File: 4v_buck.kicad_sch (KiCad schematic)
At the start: 4 parts, among them U3 MIC28517T-E/PHA

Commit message: 4v buck updates
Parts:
- added C9: 4u7F 10V, BR_Passives:C_0402_1005Metric-minimized, symbol BR_Capacitors_0402:C_0402_4u7F_10V_X7T_20%
- added L1: 10uH 10A, BR_Inductors:XR1265-100M, symbol BR_Inductors:L_XR1265-100M
- added R21: 2k2, BR_Passives:R_0402_1005Metric-minimized, symbol BR_Resistors_0402:R_0402_2k2
- added R26: 10k, BR_Passives:C_0402_1005Metric-minimized, symbol BR_Resistors_0402:R_0402_10k
- added R38: 1k74, BR_Passives:C_0402_1005Metric-minimized, symbol BR_Resistors_0402:R_0402_1k74
- added R4, R5: 2R2, BR_Passives:R_0402_1005Metric-minimized, symbol BR_Resistors_0402:R_0402_2R2
- added R6: 100k, BR_Passives:C_0402_1005Metric-minimized, symbol BR_Resistors_0402:R_0402_100k
- added R8: 51k, BR_Passives:C_0402_1005Metric-minimized, symbol BR_Resistors_0402:R_0402_51k
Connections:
- net GND: now also R38.2, R8.2
- net PGND: now also C9.2
- net PVIN: now also R4.2, R6.1
- net at C2.2, U3.12 (SW), U3.13 (SW)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: now also L1.1, R21.1
- net at U3.1 (ILIM): now also R21.2
- net at U3.21 (PVDD): now also C9.1, R5.1
- net at U3.25 (FREQ): now also R6.2, R8.1
- net at U3.27 (FB): now also R26.2, R38.1
- net at C1.1, U3.30 (VDD): now also R5.2
- net at U3.31 (SVIN): now also R4.1
- new net VOUT: L1.2, R26.1
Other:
- moved on the sheet: C1

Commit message: 4v buck updates
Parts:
- added C19: 1uF 100V, BR_Passives:C_0805_2012Metric-minimized, symbol BR_Capacitors_0805:C_0805_1uF_100V_X7S_10%
- added C20: 10nF 50V, BR_Passives:C_0402_1005Metric-minimized, symbol BR_Capacitors_0402:C_0402_10nF_50V_X7R_10%
- added C21: 100nF 100V, BR_Passives:C_0402_1005Metric-minimized, symbol BR_Capacitors_0402:C_0402_100nF_100V_X5R_20%
- added R46: 15k, BR_Passives:C_0402_1005Metric-minimized, symbol BR_Resistors_0402:R_0402_15k
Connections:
- net GND: now also C1.2, U3.26 (MODE), C19.2
- net PGND: no longer C1.2, U3.26 (MODE)
- net VOUT: now also C20.1
- net at C2.2, L1.1, R21.1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: now also R46.2
- net at R26.2, R38.1, U3.27 (FB): now also C20.2, C21.2
- net at R4.1, U3.31 (SVIN): now also C19.1
- new net: C21.1, R46.1
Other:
- moved on the sheet: C9, R4

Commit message: 4v buck complete
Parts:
- added C22, C23, C24: 2u2F 100V, BR_Passives:C_0805_2012Metric-minimized, symbol BR_Capacitors_0805:C_0805_2u2F_100V_X7T_10%
- added C25, C26: 10uF 10V, BR_Passives:C_0603_1608Metric-minimized, symbol BR_Capacitors_0603:C_0603_10uF_10V_X7T_10%
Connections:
- net PGND: now also C22.2, C23.2, C24.2, C25.2, C26.2
- net PVIN: now also C22.1, C23.1, C24.1
- net VOUT: now also C25.1, C26.1
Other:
- moved on the sheet: L1

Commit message: power scheme updates
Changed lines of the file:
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@@
+	(wire
+		(pts
+			(xy 255.27 78.74) (xy 264.16 78.74)
+		)
+		(stroke
+			(width 0)
+			(type default)
+		)
+	)
 	(wire
 		(pts
@@
 	(wire
 		(pts
+			(xy 255.27 78.74) (xy 240.03 78.74)
+		)
+		(stroke
+			(width 0)
+			(type default)
+		)
+	)
+	(wire
+		(pts
 			(xy 224.79 78.74) (xy 240.03 78.74)
 		)
@@
 	(wire
 		(pts
-			(xy 240.03 78.74) (xy 255.27 78.74)
-		)
-		(stroke
-			(width 0)
-			(type default)
-		)
-	)
-	(wire
-		(pts
 			(xy 86.36 86.36) (xy 86.36 81.28)
 		)
@@
 		(pts
 			(xy 172.72 104.14) (xy 181.61 104.14)
-		)
-		(stroke
-			(width 0)
-			(type default)
-		)
-	)
-	(wire
-		(pts
-			(xy 255.27 78.74) (xy 264.16 78.74)
 		)
 		(stroke
@@
 	)
 	(label "4V"
-		(at 227.33 78.74 0)
+		(at 259.08 78.74 0)
 		(effects
 			(font

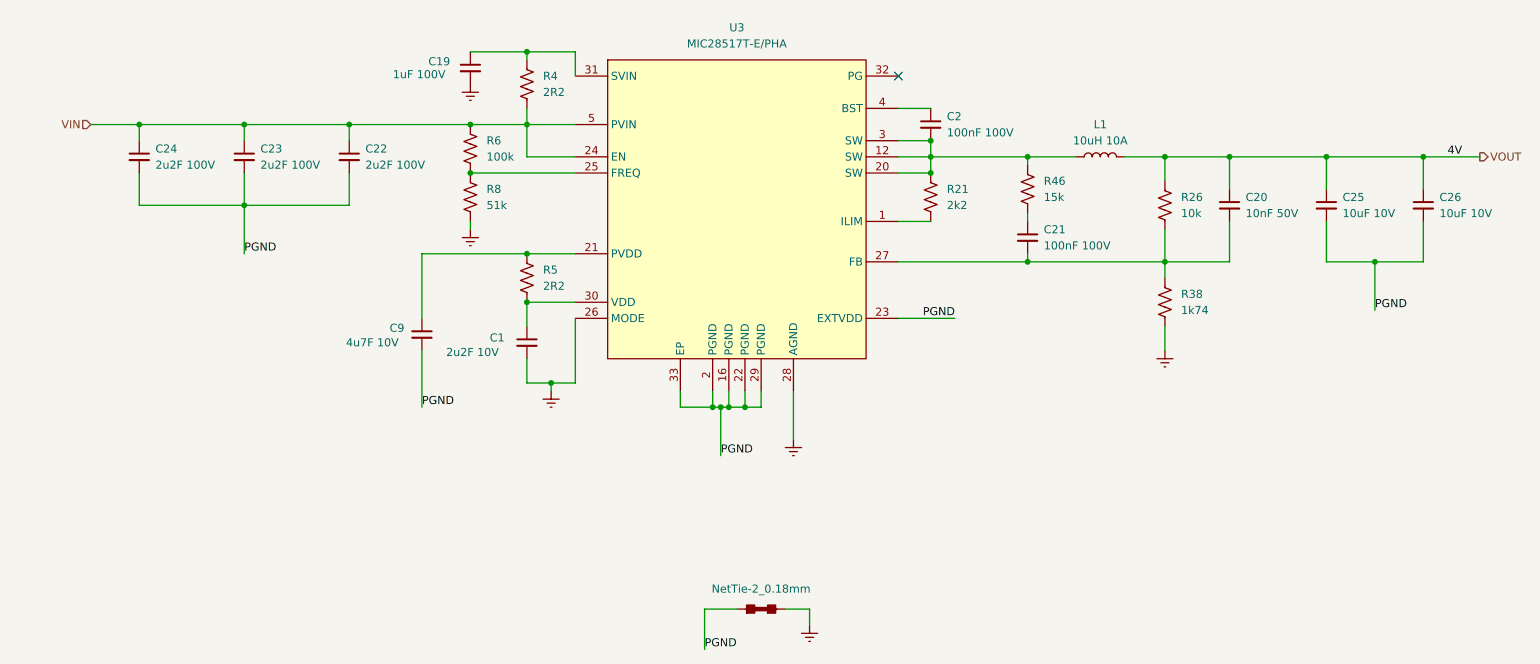
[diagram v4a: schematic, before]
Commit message: added annotations
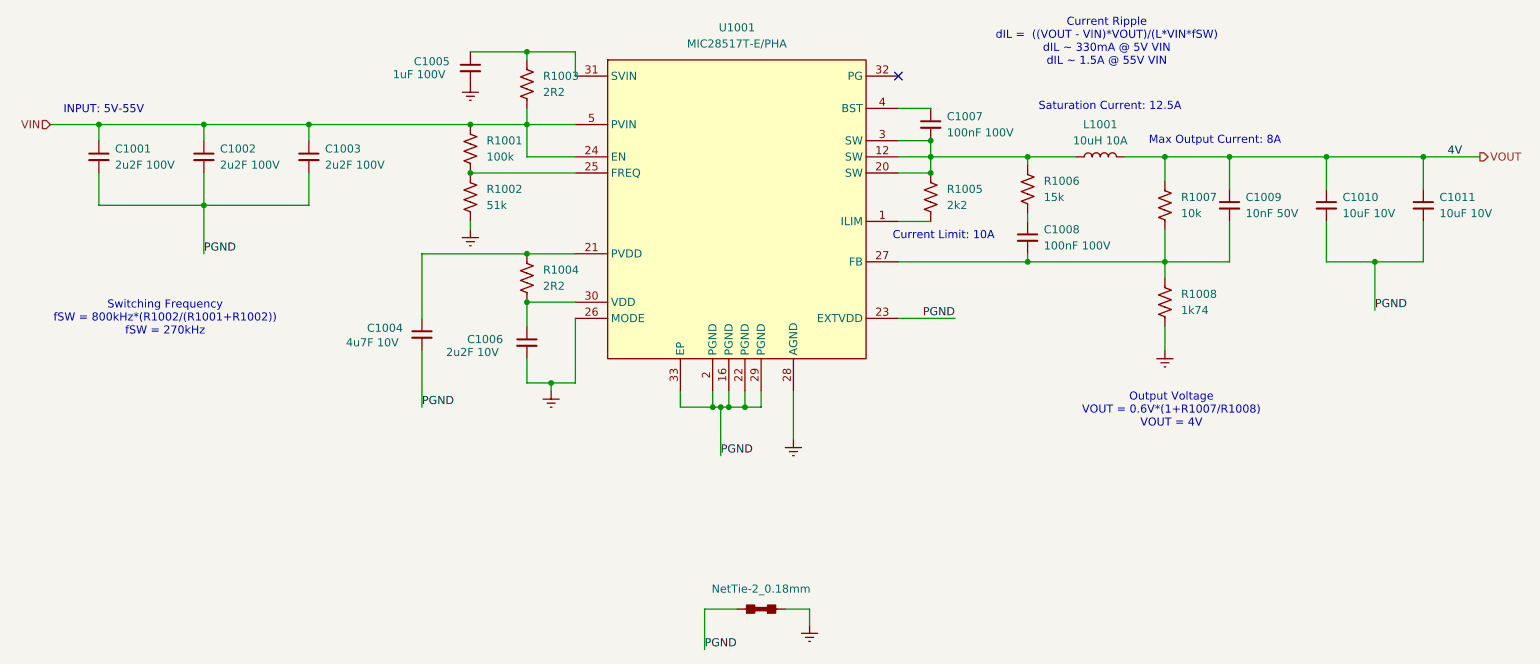
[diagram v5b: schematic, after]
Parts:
- renumbered C24 to C1001, C23 to C1002, C22 to C1003, C9 to C1004, C19 to C1005, C1 to C1006, C2 to C1007, C21 to C1008, C20 to C1009, C25 to C1010, C26 to C1011, L1 to L1001, NT1 to NT1001, R6 to R1001, R8 to R1002, R4 to R1003, R5 to R1004, R21 to R1005, R46 to R1006, R26 to R1007, R38 to R1008, U3 to U1001
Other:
- note added: "Current Limit: 10A"
- note added: "Current Ripple dIL = ((VOUT - VIN)*VOUT)/(L*VIN*fSW) dIL ~ 330mA @ 5V VIN dIL ~ 1.5A @ 55V VIN"
- note added: "INPUT: 5V-55V"
- note added: "Max Output Current: 8A"
- note added: "Output Voltage VOUT = 0.6V*(1+R1007/R1008) VOUT = 4V"
- note added: "Saturation Current: 12.5A"
- note added: "Switching Frequency fSW = 800kHz*(R1002/(R1001+R1002)) fSW = 270kHz"
- moved on the sheet: C1001, C1002, C1003

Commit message: ripple injection updates
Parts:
- C1009: value 10nF 50V -> 4n7F 100V; footprint BR_Passives:C_0402_1005Metric-minimized -> BR_Passives:C_0402_1005Metric; symbol BR_Capacitors_0402:C_0402_10nF_50V_X7R_10% -> BR_Capacitors_0402:C_0402_4n7F_100V_X7R_10%; BRE Number BRE-000013 -> BRE-000032; JLCPCB Part Num C60133 -> C415704; Manufacturer YAGEO -> Murata Electronics; Manufacturer Part Num CC0402KRX7R9BB103 -> GRM155R72A472KA01D; Supplier Part Num 1 311-1349-1-ND -> 490-3885-1-ND; Supplier Part Num 2 603-CC402KRX7R9BB103 -> 81-GRM155R72A472KA01; Supplier Part Num 3 C60133 -> C415704
- R1006: value 15k -> 24k9; symbol BR_Resistors_0402:R_0402_15k -> BR_Resistors_0402:R_0402_24k9; BRE Number BRE-000304 -> BRE-001239; JLCPCB Part Num C144795 -> C138027; Manufacturer Part Num AC0402FR-0715KL -> RC0402FR-0724K9L; Supplier Part Num 1 YAG3444CT-ND -> 311-24.9KLRCT-ND; Supplier Part Num 2 YAG3444TR-ND -> 311-24.9KLRCT-ND; Supplier Part Num 3 C144795 -> C138027
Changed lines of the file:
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@@
 	)
 	(symbol
-		(lib_id "BR_Capacitors_0402:C_0402_10nF_50V_X7R_10%")
+		(lib_id "BR_Capacitors_0402:C_0402_4n7F_100V_X7R_10%")
 		(at 224.79 86.36 0)
 		(unit 1)
@@
 			)
 		)
-		(property "Value" "10nF 50V"
+		(property "Value" "4n7F 100V"
 			(at 227.33 87.6362 0)
 			(effects
@@
 			)
 		)
-		(property "Footprint" "BR_Passives:C_0402_1005Metric-minimized"
+		(property "Footprint" "BR_Passives:C_0402_1005Metric"
 			(at 224.79 10.16 0)
 			(effects
@@
 			)
 		)
-		(property "Datasheet" "https://www.yageo.com/upload/media/product/productsearch/datasheet/mlcc/UPY-GPHC_X7R_6.3V-to-250V_23.pdf"
+		(property "Datasheet" "https://www.lcsc.com/datasheet/lcsc_datasheet_2304140030_Murata-Electronics-GRM155R72A472KA01D_C415704.pdf"
 			(at 224.79 12.7 0)
 			(effects
@@
 			)
 		)
-		(property "Description" "10nF 50V X7R 10% Ceramic Capacitor 0402"
+		(property "Description" "4.7nF 100V X7R 10% Ceramic Capacitor 0402"
+			(at 224.79 22.86 0)
+			(effects
+				(font
+					(size 1.27 1.27)
+				)
+				(justify left)
+				(hide yes)
+			)
+		)
+		(property "Manufacturer" "Murata Electronics"
 			(at 224.79 15.24 0)
 			(effects
@@
 			)
 		)
-		(property "Manufacturer" "YAGEO"
+		(property "Manufacturer Part Num" "GRM155R72A472KA01D"
 			(at 224.79 17.78 0)
 			(effects
@@
 			)
 		)
-		(property "Manufacturer Part Num" "CC0402KRX7R9BB103"
+		(property "BRE Number" "BRE-000032"
 			(at 224.79 20.32 0)
-			(effects
-				(font
-					(size 1.27 1.27)
-				)
-				(justify left)
-				(hide yes)
-			)
-		)
-		(property "BRE Number" "BRE-000013"
-			(at 224.79 22.86 0)
 			(effects
 				(font
@@
 			)
 		)
-		(property "Supplier Part Num 1" "311-1349-1-ND"
+		(property "Supplier Part Num 1" "490-3885-1-ND"
 			(at 224.79 27.94 0)
 			(effects
@@
 			)
 		)
-		(property "Supplier Part Num 2" "603-CC402KRX7R9BB103"
+		(property "Supplier Part Num 2" "81-GRM155R72A472KA01"
 			(at 224.79 33.02 0)
 			(effects
@@
 			)
 		)
-		(property "Supplier Part Num 3" "C60133"
+		(property "Supplier Part Num 3" "C415704"
 			(at 224.79 38.1 0)
 			(effects
@@
 			)
 		)
-		(property "JLCPCB Part Num" "C60133"
-			(at 224.79 40.64 0)
+		(property "JLCPCB Part Num" "C415704"
+			(at 224.79 45.72 0)
 			(effects
 				(font
@@
 		(on_board yes)
 		(dnp no)
-		(fields_autoplaced yes)
 		(property "Reference" "R1003"
-			(at 116.84 66.0399 0)
+			(at 116.84 67.818 0)
 			(effects
 				(font
@@
 		)
 		(property "Value" "2R2"
-			(at 116.84 68.5799 0)
+			(at 116.84 70.358 0)
 			(effects
 				(font
@@
 	)
 	(symbol
-		(lib_id "BR_Resistors_0402:R_0402_15k")
+		(lib_id "BR_Resistors_0402:R_0402_24k9")
 		(at 193.04 83.82 180)
 		(unit 1)
@@
 			)
 		)
-		(property "Value" "15k"
+		(property "Value" "24k9"
 			(at 195.58 85.0899 0)
 			(effects
@@
 			)
 		)
-		(property "Datasheet" "https://www.yageo.com/upload/media/product/productsearch/datasheet/rchip/PYu-AC_51_RoHS_L_10.pdf"
+		(property "Datasheet" "https://www.yageo.com/upload/media/product/products/datasheet/rchip/PYu-RC_Group_51_RoHS_L_12.pdf"
 			(at 193.04 157.48 0)
 			(effects
@@
 			)
 		)
-		(property "Description" "15k 1% 100ppm 62.5mW Thick Film Resistor 0402"
+		(property "Description" "24.9k 1% 100ppm 62.5mW Thick Film Resistor 0402"
 			(at 193.04 154.94 0)
 			(effects
@@
 			)
 		)
-		(property "Manufacturer Part Num" "AC0402FR-0715KL"
+		(property "Manufacturer Part Num" "RC0402FR-0724K9L"
 			(at 193.04 149.86 0)
 			(effects
@@
 			)
 		)
-		(property "BRE Number" "BRE-000304"
+		(property "BRE Number" "BRE-001239"
 			(at 193.04 147.32 0)
 			(effects
@@
 			)
 		)
-		(property "Supplier Part Num 1" "YAG3444CT-ND"
+		(property "Supplier Part Num 1" "311-24.9KLRCT-ND"
 			(at 193.04 142.24 0)
 			(effects
@@
 			)
 		)
-		(property "Supplier Part Num 2" "YAG3444TR-ND"
+		(property "Supplier Part Num 2" "311-24.9KLRCT-ND"
 			(at 193.04 137.16 0)
 			(effects
@@
 			)
 		)
-		(property "Supplier Part Num 3" "C144795"
+		(property "Supplier Part Num 3" "C138027"
 			(at 193.04 132.08 0)
 			(effects
@@
 			)
 		)
-		(property "JLCPCB Part Num" "C144795"
+		(property "JLCPCB Part Num" "C138027"
 			(at 193.04 129.54 0)
 			(effects

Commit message: power updates
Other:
- note added: "Current Ripple dIL = ((VIN - VOUT)*VOUT)/(L*VIN*fSW) dIL ~ 330mA @ 5V VIN dIL ~ 1.5A @ 55V VIN"
- note removed: "Current Ripple dIL = ((VOUT - VIN)*VOUT)/(L*VIN*fSW) dIL ~ 330mA @ 5V VIN dIL ~ 1.5A @ 55V VIN"
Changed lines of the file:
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@@
 		)
 	)
-	(text "Current Ripple\ndIL =  ((VOUT - VIN)*VOUT)/(L*VIN*fSW)\ndIL ~ 330mA @ 5V VIN\ndIL ~ 1.5A @ 55V VIN"
+	(text "Current Ripple\ndIL =  ((VIN - VOUT)*VOUT)/(L*VIN*fSW)\ndIL ~ 330mA @ 5V VIN\ndIL ~ 1.5A @ 55V VIN"
 		(exclude_from_sim no)
 		(at 205.486 60.706 0)

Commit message: rewiring STM32H563
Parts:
- R1007: value 10k -> 4k99; symbol BR_Resistors_0402:R_0402_10k -> BR_Resistors_0402:R_0402_4k99; BRE Number BRE-000292 -> BRE-000353; JLCPCB Part Num C144807 -> C137965; Manufacturer Part Num AC0402FR-0710KL -> RC0402FR-074K99L; Supplier Part Num 1 YAG3436CT-ND -> 311-4.99KLRCT-ND; Supplier Part Num 2 YAG3436TR-ND -> 311-4.99KLRTR-ND; Supplier Part Num 3 C144807 -> C137965
- R1008: value 1k74 -> 681R; symbol BR_Resistors_0402:R_0402_1k74 -> BR_Resistors_0402:R_0402_681R; BRE Number BRE-001233 -> BRE-000364; JLCPCB Part Num C163482 -> C245891; Manufacturer Part Num RC0402FR-071K74L -> RC0402FR-07681RL; Supplier 2 DigiKey -> Mouser; Supplier Part Num 1 YAG3046CT-ND -> YAG2375CT-ND; Supplier Part Num 2 YAG3046CT-ND -> 603-RC0402FR-07681RL; Supplier Part Num 3 C163482 -> C245891
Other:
- note added: "Current Ripple dIL = ((VIN - VOUT)*VOUT)/(L*VIN*fSW) dIL ~ 170mA @ 5V5 VIN dIL ~ 1.7A @ 55V VIN"
- note added: "INPUT: 5V5-55V"
- note added: "Output Voltage VOUT = 0.6V*(1+R1007/R1008) VOUT = 5V"
- note removed: "Current Ripple dIL = ((VIN - VOUT)*VOUT)/(L*VIN*fSW) dIL ~ 330mA @ 5V VIN dIL ~ 1.5A @ 55V VIN"
- note removed: "INPUT: 5V-55V"
- note removed: "Output Voltage VOUT = 0.6V*(1+R1007/R1008) VOUT = 4V"
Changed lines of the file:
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@@
 	(generator_version "9.0")
 	(paper "A4")
-	(text "Output Voltage\nVOUT = 0.6V*(1+R1007/R1008)\nVOUT = 4V"
+	(text "Output Voltage\nVOUT = 0.6V*(1+R1007/R1008)\nVOUT = 5V"
 		(exclude_from_sim no)
 		(at 215.646 118.618 0)
@@
 		)
 	)
-	(text "INPUT: 5V-55V"
+	(text "INPUT: 5V5-55V"
 		(exclude_from_sim no)
 		(at 47.752 71.374 0)
@@
 		)
 	)
-	(text "Current Ripple\ndIL =  ((VIN - VOUT)*VOUT)/(L*VIN*fSW)\ndIL ~ 330mA @ 5V VIN\ndIL ~ 1.5A @ 55V VIN"
+	(text "Current Ripple\ndIL =  ((VIN - VOUT)*VOUT)/(L*VIN*fSW)\ndIL ~ 170mA @ 5V5 VIN\ndIL ~ 1.7A @ 55V VIN"
 		(exclude_from_sim no)
 		(at 205.486 60.706 0)
@@
 		)
 	)
-	(label "4V"
+	(label "5V"
 		(at 259.08 78.74 0)
 		(effects
@@
 	)
 	(symbol
-		(lib_id "BR_Resistors_0402:R_0402_10k")
+		(lib_id "BR_Resistors_0402:R_0402_4k99")
 		(at 214.63 86.36 0)
 		(unit 1)
@@
 			)
 		)
-		(property "Value" "10k"
+		(property "Value" "4k99"
 			(at 217.17 87.6299 0)
 			(effects
@@
 			)
 		)
-		(property "Datasheet" "https://www.yageo.com/upload/media/product/productsearch/datasheet/rchip/PYu-AC_51_RoHS_L_10.pdf"
+		(property "Datasheet" "https://www.yageo.com/upload/media/product/productsearch/datasheet/rchip/PYu-RC_Group_51_RoHS_L_12.pdf"
 			(at 214.63 12.7 0)
 			(effects
@@
 			)
 		)
-		(property "Description" "10k 1% 100ppm 62.5mW Thick Film Resistor 0402"
+		(property "Description" "4.99k 1% 100ppm 62.5mW Thick Film Resistor 0402"
 			(at 214.63 15.24 0)
 			(effects
@@
 			)
 		)
-		(property "Manufacturer Part Num" "AC0402FR-0710KL"
+		(property "Manufacturer Part Num" "RC0402FR-074K99L"
 			(at 214.63 20.32 0)
 			(effects
@@
 			)
 		)
-		(property "BRE Number" "BRE-000292"
+		(property "BRE Number" "BRE-000353"
 			(at 214.63 22.86 0)
 			(effects
@@
 			)
 		)
-		(property "Supplier Part Num 1" "YAG3436CT-ND"
+		(property "Supplier Part Num 1" "311-4.99KLRCT-ND"
 			(at 214.63 27.94 0)
 			(effects
@@
 			)
 		)
-		(property "Supplier Part Num 2" "YAG3436TR-ND"
+		(property "Supplier Part Num 2" "311-4.99KLRTR-ND"
 			(at 214.63 33.02 0)
 			(effects
@@
 			)
 		)
-		(property "Supplier Part Num 3" "C144807"
+		(property "Supplier Part Num 3" "C137965"
 			(at 214.63 38.1 0)
 			(effects
@@
 			)
 		)
-		(property "JLCPCB Part Num" "C144807"
+		(property "JLCPCB Part Num" "C137965"
 			(at 214.63 40.64 0)
 			(effects
@@
 	)
 	(symbol
-		(lib_id "BR_Resistors_0402:R_0402_1k74")
+		(lib_id "BR_Resistors_0402:R_0402_681R")
 		(at 214.63 101.6 0)
 		(unit 1)
@@
 			)
 		)
-		(property "Value" "1k74"
+		(property "Value" "681R"
 			(at 217.17 102.8699 0)
 			(effects
@@
 			)
 		)
-		(property "Description" "1.74k 1% 100ppm 62.5mW Thick Film Resistor 0402"
+		(property "Description" "681R 1% 100ppm 62.5mW Thick Film Resistor 0402"
 			(at 214.63 30.48 0)
 			(effects
@@
 			)
 		)
-		(property "Manufacturer Part Num" "RC0402FR-071K74L"
+		(property "Manufacturer Part Num" "RC0402FR-07681RL"
 			(at 214.63 35.56 0)
 			(effects
@@
 			)
 		)
-		(property "BRE Number" "BRE-001233"
+		(property "BRE Number" "BRE-000364"
 			(at 214.63 38.1 0)
 			(effects
@@
 			)
 		)
-		(property "Supplier Part Num 1" "YAG3046CT-ND"
+		(property "Supplier Part Num 1" "YAG2375CT-ND"
 			(at 214.63 43.18 0)
 			(effects
@@
 			)
 		)
-		(property "Supplier 2" "DigiKey"
+		(property "Supplier 2" "Mouser"
 			(at 214.63 45.72 0)
 			(effects
@@
 			)
 		)
-		(property "Supplier Part Num 2" "YAG3046CT-ND"
+		(property "Supplier Part Num 2" "603-RC0402FR-07681RL"
 			(at 214.63 48.26 0)
 			(effects
@@
 			)
 		)
-		(property "Supplier Part Num 3" "C163482"
+		(property "Supplier Part Num 3" "C245891"
 			(at 214.63 53.34 0)
 			(effects
@@
 			)
 		)
-		(property "JLCPCB Part Num" "C163482"
+		(property "JLCPCB Part Num" "C245891"
 			(at 214.63 55.88 0)
 			(effects
